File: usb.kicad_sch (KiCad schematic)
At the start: 20 parts, among them J12 USB_A, J3 2169900003, Q1 MMBT3904, U12 STMPS2141STR

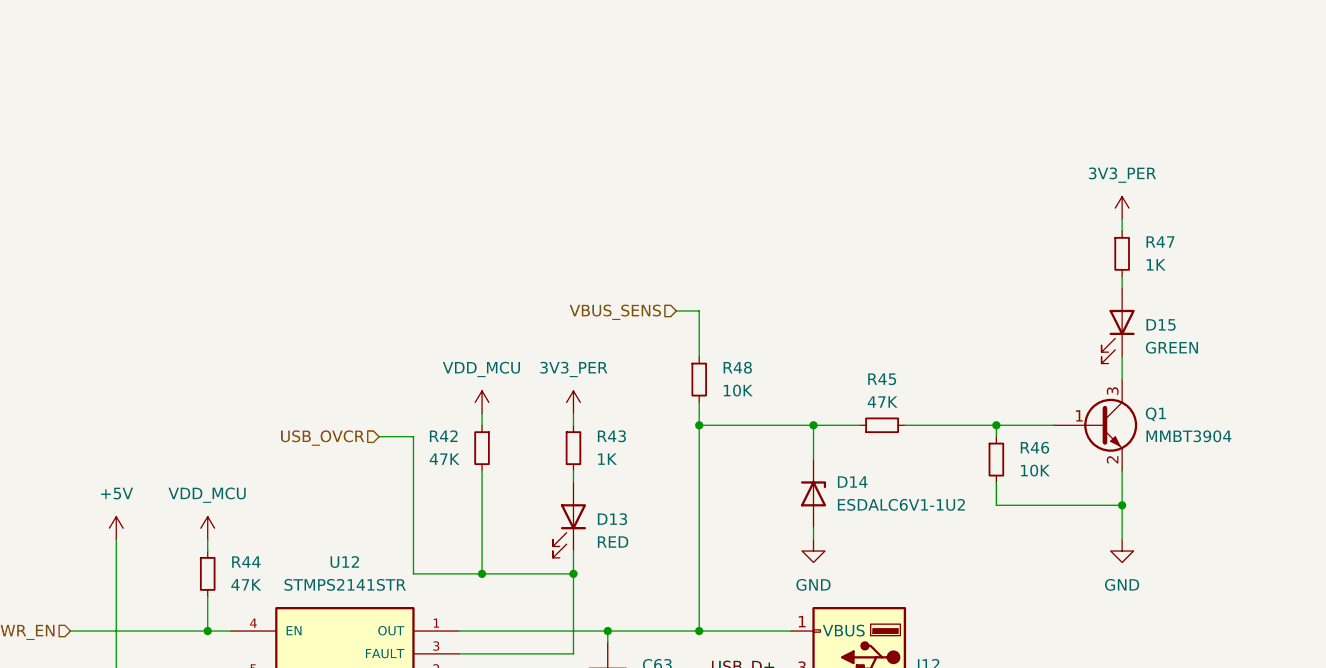
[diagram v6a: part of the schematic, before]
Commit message: Removing Camera, create alternative footprint for SPI LCD conn
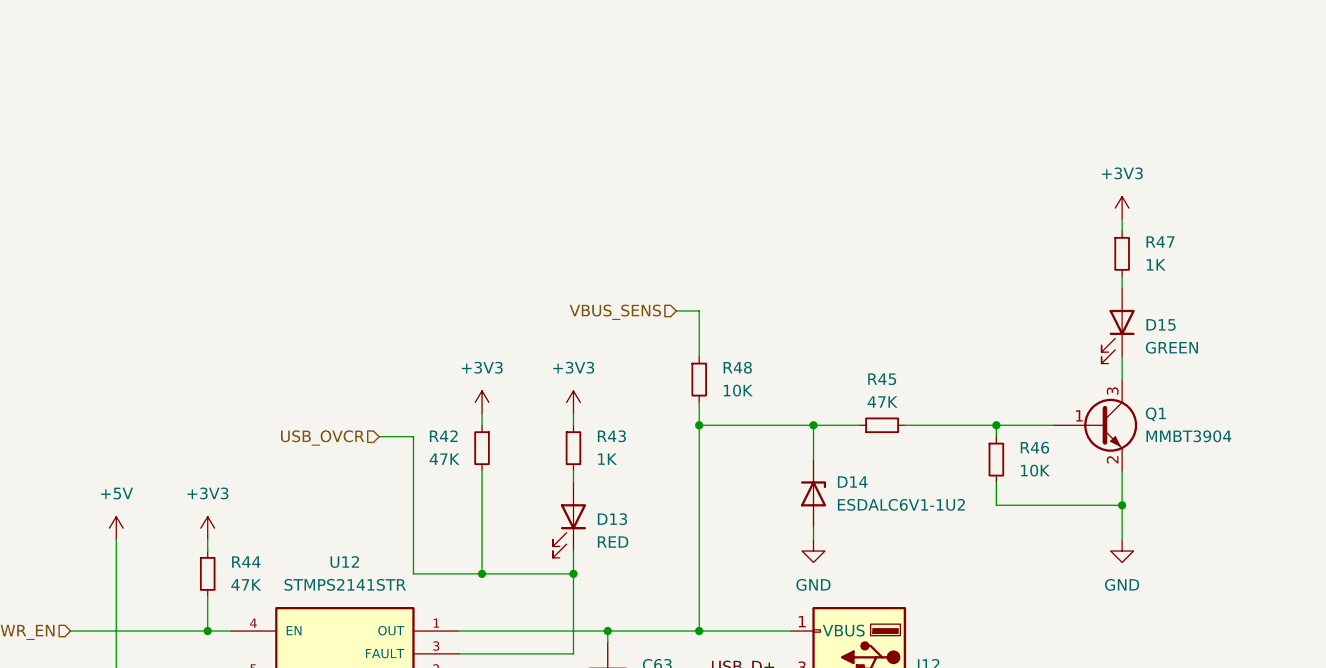
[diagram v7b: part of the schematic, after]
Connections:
- net VDD_MCU is gone; now on net +3V3: R42.1, R44.1
- net 3V3_PER renamed +3V3
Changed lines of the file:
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@@
+	)
+	(symbol
+		(lib_name "+3V3_1")
+		(lib_id "power:+3V3")
+		(at 166.37 67.31 0)
+		(unit 1)
+		(exclude_from_sim no)
+		(in_bom yes)
+		(on_board yes)
+		(dnp no)
+		(fields_autoplaced yes)
+		(property "Reference" "#PWR0142"
+			(at 166.37 71.12 0)
+			(effects
+				(font
+					(size 1.27 1.27)
+				)
+				(hide yes)
+			)
+		)
+		(property "Value" "+3V3"
+			(at 166.37 62.23 0)
+			(effects
+				(font
+					(size 1.27 1.27)
+				)
+			)
+		)
+		(property "Footprint" ""
+			(at 166.37 67.31 0)
+			(effects
+				(font
+					(size 1.27 1.27)
+				)
+				(hide yes)
+			)
+		)
+		(property "Datasheet" ""
+			(at 166.37 67.31 0)
+			(effects
+				(font
+					(size 1.27 1.27)
+				)
+				(hide yes)
+			)
+		)
+		(property "Description" "Power symbol creates a global label with name \"+3V3\""
+			(at 166.37 67.31 0)
+			(effects
+				(font
+					(size 1.27 1.27)
+				)
+				(hide yes)
+			)
+		)
+		(pin "1"
+		)
+		(instances
+			(project "chroma-pixel-zeta"
+				(path "/70094798-b7e4-48a4-a512-b8f48be18f9f/87d5fb8c-ace9-453f-ab56-153ed16cc12a"
+					(reference "#PWR0142")
+					(unit 1)
+				)
+			)
+		)
 	)
 	(symbol
@@
 	)
 	(symbol
-		(lib_id "power:+5V")
-		(at 166.37 67.31 0)
-		(unit 1)
-		(exclude_from_sim no)
-		(in_bom yes)
-		(on_board yes)
-		(dnp no)
-		(fields_autoplaced yes)
-		(property "Reference" "#PWR0146"
-			(at 166.37 71.12 0)
-			(effects
-				(font
-					(size 1.27 1.27)
-				)
-				(hide yes)
-			)
-		)
-		(property "Value" "3V3_PER"
-			(at 166.37 62.23 0)
-			(effects
-				(font
-					(size 1.27 1.27)
-				)
-			)
-		)
-		(property "Footprint" ""
-			(at 166.37 67.31 0)
-			(effects
-				(font
-					(size 1.27 1.27)
-				)
-				(hide yes)
-			)
-		)
-		(property "Datasheet" ""
-			(at 166.37 67.31 0)
-			(effects
-				(font
-					(size 1.27 1.27)
-				)
-				(hide yes)
-			)
-		)
-		(property "Description" "Power symbol creates a global label with name \"+5V\""
-			(at 166.37 67.31 0)
-			(effects
-				(font
-					(size 1.27 1.27)
-				)
-				(hide yes)
-			)
-		)
-		(pin "1"
-		)
-		(instances
-			(project "chroma-pixel-zeta"
-				(path "/70094798-b7e4-48a4-a512-b8f48be18f9f/87d5fb8c-ace9-453f-ab56-153ed16cc12a"
-					(reference "#PWR0146")
-					(unit 1)
-				)
-			)
-		)
-	)
-	(symbol
 		(lib_id "Device:LED")
 		(at 105.41 100.33 270)
@@
 				(path "/70094798-b7e4-48a4-a512-b8f48be18f9f/87d5fb8c-ace9-453f-ab56-153ed16cc12a"
 					(reference "D13")
+					(unit 1)
+				)
+			)
+		)
+	)
+	(symbol
+		(lib_name "+3V3_1")
+		(lib_id "power:+3V3")
+		(at 105.41 88.9 0)
+		(unit 1)
+		(exclude_from_sim no)
+		(in_bom yes)
+		(on_board yes)
+		(dnp no)
+		(fields_autoplaced yes)
+		(property "Reference" "#PWR069"
+			(at 105.41 92.71 0)
+			(effects
+				(font
+					(size 1.27 1.27)
+				)
+				(hide yes)
+			)
+		)
+		(property "Value" "+3V3"
+			(at 105.41 83.82 0)
+			(effects
+				(font
+					(size 1.27 1.27)
+				)
+			)
+		)
+		(property "Footprint" ""
+			(at 105.41 88.9 0)
+			(effects
+				(font
+					(size 1.27 1.27)
+				)
+				(hide yes)
+			)
+		)
+		(property "Datasheet" ""
+			(at 105.41 88.9 0)
+			(effects
+				(font
+					(size 1.27 1.27)
+				)
+				(hide yes)
+			)
+		)
+		(property "Description" "Power symbol creates a global label with name \"+3V3\""
+			(at 105.41 88.9 0)
+			(effects
+				(font
+					(size 1.27 1.27)
+				)
+				(hide yes)
+			)
+		)
+		(pin "1"
+		)
+		(instances
+			(project "chroma-pixel-zeta"
+				(path "/70094798-b7e4-48a4-a512-b8f48be18f9f/87d5fb8c-ace9-453f-ab56-153ed16cc12a"
+					(reference "#PWR069")
 					(unit 1)
 				)
@@
 	)
 	(symbol
+		(lib_name "+3V3_1")
 		(lib_id "power:+3V3")
-		(at 95.25 88.9 0)
-		(mirror y)
+		(at 64.77 102.87 0)
 		(unit 1)
 		(exclude_from_sim no)
@@
 		(dnp no)
 		(fields_autoplaced yes)
-		(property "Reference" "#PWR0142"
-			(at 95.25 92.71 0)
-			(effects
-				(font
-					(size 1.27 1.27)
-				)
-				(hide yes)
-			)
-		)
-		(property "Value" "VDD_MCU"
-			(at 95.25 83.82 0)
+		(property "Reference" "#PWR0140"
+			(at 64.77 106.68 0)
+			(effects
+				(font
+					(size 1.27 1.27)
+				)
+				(hide yes)
+			)
+		)
+		(property "Value" "+3V3"
+			(at 64.77 97.79 0)
 			(effects
 				(font
@@
 		)
 		(property "Footprint" ""
-			(at 95.25 88.9 0)
+			(at 64.77 102.87 0)
 			(effects
 				(font
@@
 		)
 		(property "Datasheet" ""
-			(at 95.25 88.9 0)
+			(at 64.77 102.87 0)
 			(effects
 				(font
@@
 		)
 		(property "Description" "Power symbol creates a global label with name \"+3V3\""
-			(at 95.25 88.9 0)
+			(at 64.77 102.87 0)
 			(effects
 				(font
@@
 			(project "chroma-pixel-zeta"
 				(path "/70094798-b7e4-48a4-a512-b8f48be18f9f/87d5fb8c-ace9-453f-ab56-153ed16cc12a"
-					(reference "#PWR0142")
+					(reference "#PWR0140")
 					(unit 1)
 				)
@@
 	)
 	(symbol
+		(lib_name "+3V3_1")
 		(lib_id "power:+3V3")
-		(at 64.77 102.87 0)
+		(at 95.25 88.9 0)
 		(unit 1)
 		(exclude_from_sim no)
@@
 		(dnp no)
 		(fields_autoplaced yes)
-		(property "Reference" "#PWR0140"
-			(at 64.77 106.68 0)
-			(effects
-				(font
-					(size 1.27 1.27)
-				)
-				(hide yes)
-			)
-		)
-		(property "Value" "VDD_MCU"
-			(at 64.77 97.79 0)
+		(property "Reference" "#PWR0162"
+			(at 95.25 92.71 0)
+			(effects
+				(font
+					(size 1.27 1.27)
+				)
+				(hide yes)
+			)
+		)
+		(property "Value" "+3V3"
+			(at 95.25 83.82 0)
 			(effects
 				(font
@@
 		)
 		(property "Footprint" ""
-			(at 64.77 102.87 0)
+			(at 95.25 88.9 0)
 			(effects
 				(font
@@
 		)
 		(property "Datasheet" ""
-			(at 64.77 102.87 0)
+			(at 95.25 88.9 0)
 			(effects
 				(font
@@
 		)
 		(property "Description" "Power symbol creates a global label with name \"+3V3\""
-			(at 64.77 102.87 0)
+			(at 95.25 88.9 0)
 			(effects
 				(font
@@
 			(project "chroma-pixel-zeta"
 				(path "/70094798-b7e4-48a4-a512-b8f48be18f9f/87d5fb8c-ace9-453f-ab56-153ed16cc12a"
-					(reference "#PWR0140")
+					(reference "#PWR0162")
 					(unit 1)
 				)
@@
 					(unit 1)
 				)
-			)
-		)
-	)
-	(symbol
-		(lib_id "power:+5V")
-		(at 105.41 88.9 0)
-		(unit 1)
-		(exclude_from_sim no)
-		(in_bom yes)
-		(on_board yes)
-		(dnp no)
-		(fields_autoplaced yes)
-		(property "Reference" "#PWR069"
-			(at 105.41 92.71 0)
-			(effects
-				(font
-					(size 1.27 1.27)
-				)
-				(hide yes)
-			)
-		)
-		(property "Value" "3V3_PER"
-			(at 105.41 83.82 0)
-			(effects
-				(font
-					(size 1.27 1.27)
-				)
-			)
-		)
-		(property "Footprint" ""
-			(at 105.41 88.9 0)
-			(effects
-				(font
-					(size 1.27 1.27)
-				)
-				(hide yes)
-			)
-		)
-		(property "Datasheet" ""
-			(at 105.41 88.9 0)
-			(effects
-				(font
-					(size 1.27 1.27)
-				)
-				(hide yes)
-			)
-		)
-		(property "Description" "Power symbol creates a global label with name \"+5V\""
-			(at 105.41 88.9 0)
-			(effects
-				(font
-					(size 1.27 1.27)
-				)
-				(hide yes)
-			)
-		)
-		(pin "1"
-		)
-		(instances
-			(project "chroma-pixel-zeta"
-				(path "/70094798-b7e4-48a4-a512-b8f48be18f9f/87d5fb8c-ace9-453f-ab56-153ed16cc12a"
-					(reference "#PWR069")
-					(unit 1)
-				)

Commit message: First release
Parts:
- C63: value 4u7 -> 4u7/0805
- D14: JLCPCB Part # (none) -> C1974498; now left out of the parts list
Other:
- moved on the sheet: C63
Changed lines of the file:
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@@
 	(wire
 		(pts
-			(xy 109.22 121.92) (xy 109.22 123.19)
+			(xy 109.22 128.27) (xy 109.22 129.54)
 		)
 		(stroke
@@
 	(wire
 		(pts
-			(xy 109.22 113.03) (xy 109.22 114.3)
+			(xy 109.22 113.03) (xy 109.22 120.65)
 		)
 		(stroke
@@
 	(symbol
 		(lib_id "Device:C")
-		(at 109.22 118.11 0)
+		(at 109.22 124.46 0)
 		(unit 1)
 		(exclude_from_sim no)
@@
 		(fields_autoplaced yes)
 		(property "Reference" "C63"
-			(at 113.03 116.8399 0)
+			(at 113.03 123.1899 0)
 			(effects
 				(font
@@
 			)
 		)
-		(property "Value" "4u7"
-			(at 113.03 119.3799 0)
+		(property "Value" "4u7/0805"
+			(at 113.03 125.7299 0)
 			(effects
 				(font
@@
 		)
 		(property "Footprint" "Capacitor_SMD:C_0805_2012Metric"
-			(at 110.1852 121.92 0)
+			(at 110.1852 128.27 0)
 			(effects
 				(font
@@
 		)
 		(property "Datasheet" "~"
-			(at 109.22 118.11 0)
+			(at 109.22 124.46 0)
 			(effects
 				(font
@@
 		)
 		(property "Description" "Unpolarized capacitor"
-			(at 109.22 118.11 0)
+			(at 109.22 124.46 0)
 			(effects
 				(font
@@
 		)
 		(property "JLCPCB Part #" "C98192"
-			(at 109.22 118.11 0)
+			(at 109.22 124.46 0)
 			(effects
 				(font
@@
 		)
 		(property "Arrow Part Number" ""
-			(at 109.22 118.11 0)
+			(at 109.22 124.46 0)
 			(effects
 				(font
@@
 		)
 		(property "Arrow Price/Stock" ""
-			(at 109.22 118.11 0)
+			(at 109.22 124.46 0)
 			(effects
 				(font
@@
 		)
 		(property "Height" ""
-			(at 109.22 118.11 0)
+			(at 109.22 124.46 0)
 			(effects
 				(font
@@
 		)
 		(property "Manufacturer_Name" ""
-			(at 109.22 118.11 0)
+			(at 109.22 124.46 0)
 			(effects
 				(font
@@
 		)
 		(property "Manufacturer_Part_Number" ""
-			(at 109.22 118.11 0)
+			(at 109.22 124.46 0)
 			(effects
 				(font
@@
 		)
 		(property "Mouser Part Number" ""
-			(at 109.22 118.11 0)
+			(at 109.22 124.46 0)
 			(effects
 				(font
@@
 		)
 		(property "Mouser Price/Stock" ""
-			(at 109.22 118.11 0)
+			(at 109.22 124.46 0)
 			(effects
 				(font
@@
 	(symbol
 		(lib_id "power:GND")
-		(at 109.22 123.19 0)
+		(at 109.22 129.54 0)
 		(unit 1)
 		(exclude_from_sim no)
@@
 		(fields_autoplaced yes)
 		(property "Reference" "#PWR0143"
-			(at 109.22 129.54 0)
+			(at 109.22 135.89 0)
 			(effects
 				(font
@@
 		)
 		(property "Value" "GND"
-			(at 109.22 128.27 0)
+			(at 109.22 134.62 0)
 			(effects
 				(font
@@
 		)
 		(property "Footprint" ""
-			(at 109.22 123.19 0)
+			(at 109.22 129.54 0)
 			(effects
 				(font
@@
 		)
 		(property "Datasheet" ""
-			(at 109.22 123.19 0)
+			(at 109.22 129.54 0)
 			(effects
 				(font
@@
 		)
 		(property "Description" "Power symbol creates a global label with name \"GND\" , ground"
-			(at 109.22 123.19 0)
+			(at 109.22 129.54 0)
 			(effects
 				(font
@@
 		(unit 1)
 		(exclude_from_sim no)
-		(in_bom yes)
+		(in_bom no)
 		(on_board yes)
 		(dnp no)
@@
 			(at 132.08 97.79 0)
 			(effects
+				(font
+					(size 1.27 1.27)
+				)
+				(hide yes)
+			)
+		)
+		(property "JLCPCB Part #" "C1974498"
+			(at 132.08 97.79 0)
+			(effects
